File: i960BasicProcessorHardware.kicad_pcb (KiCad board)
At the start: 4 copper layers, 169.9 x 169.8 mm, 75 parts, among them J1 Conn_01x08, J10 Conn_02x39_Odd_Even, J12 Conn_01x03, J13 AVR-ISP-6, J14 Conn_01x06 (Serial Connector), J15 Conn_01x01, J2 Conn_02x05_Odd_Even, J3 Conn_02x05_Odd_Even, J4 Conn_02x05_Odd_Even, J5 Conn_02x16_Odd_Even, J6 Conn_01x03, J7 Conn_01x03, J8 Conn_01x03, J9 Conn_01x11, U1 74HC245, U10 Adafruit_FeatherWing (PSRAM F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, U11 Adafruit_FeatherWing (PSRAM F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, U12 74LS125, U13 74LS04, U14 74LS08, U15 74LS174, U16 SN74LVC245AN, U17 74LS174, U18 ATmega1284P-PU, U2 80960Sx, U3 MCP23S17_SP, U4 MCP23S17_SP, U5 74HC245, U6 74HC573, U7 74HC573, U8 MCP23S17_SP, U9 MCP23S17_SP, X1 CXO_DIP14

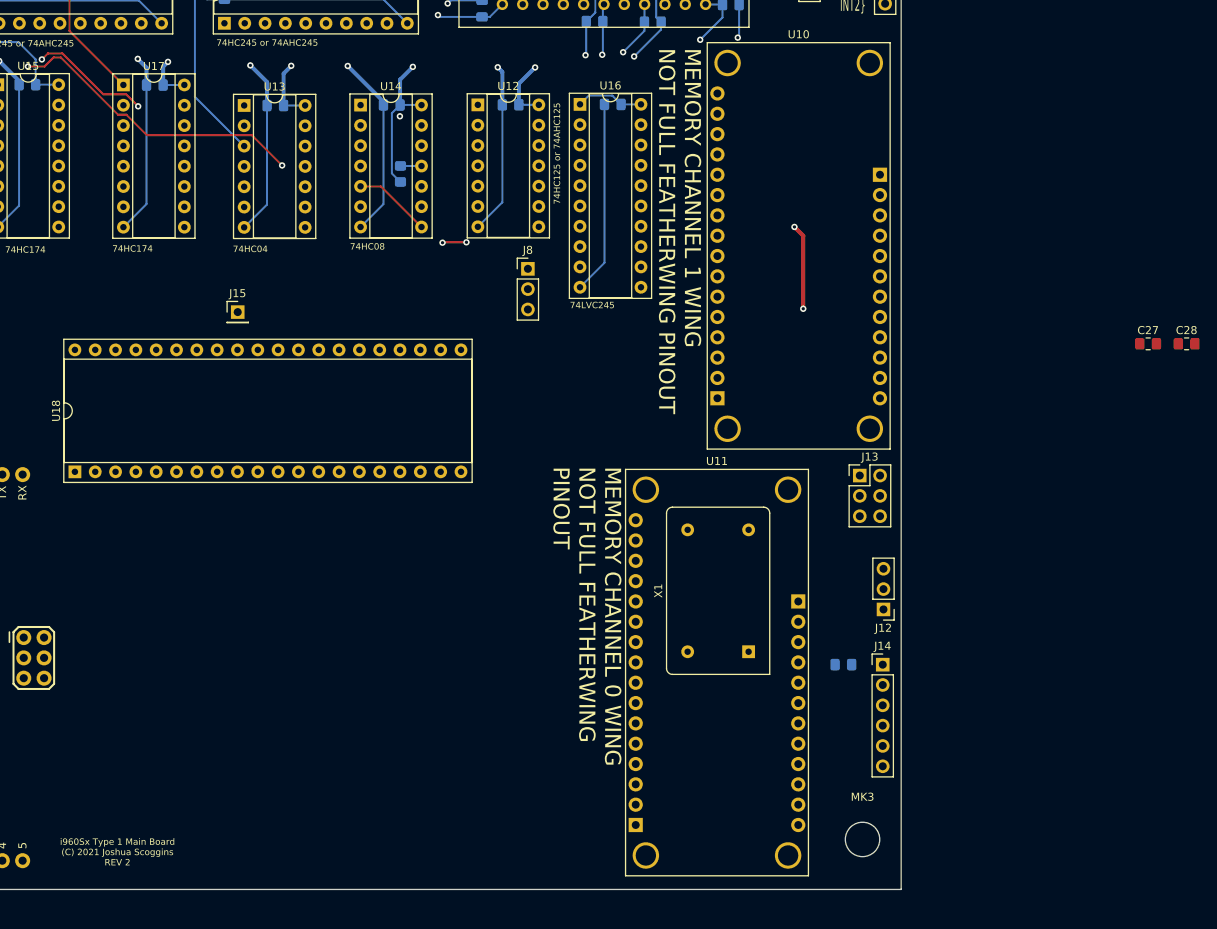
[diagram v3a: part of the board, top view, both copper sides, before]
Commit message: Double headers for each co processor
Added a second coprocessor
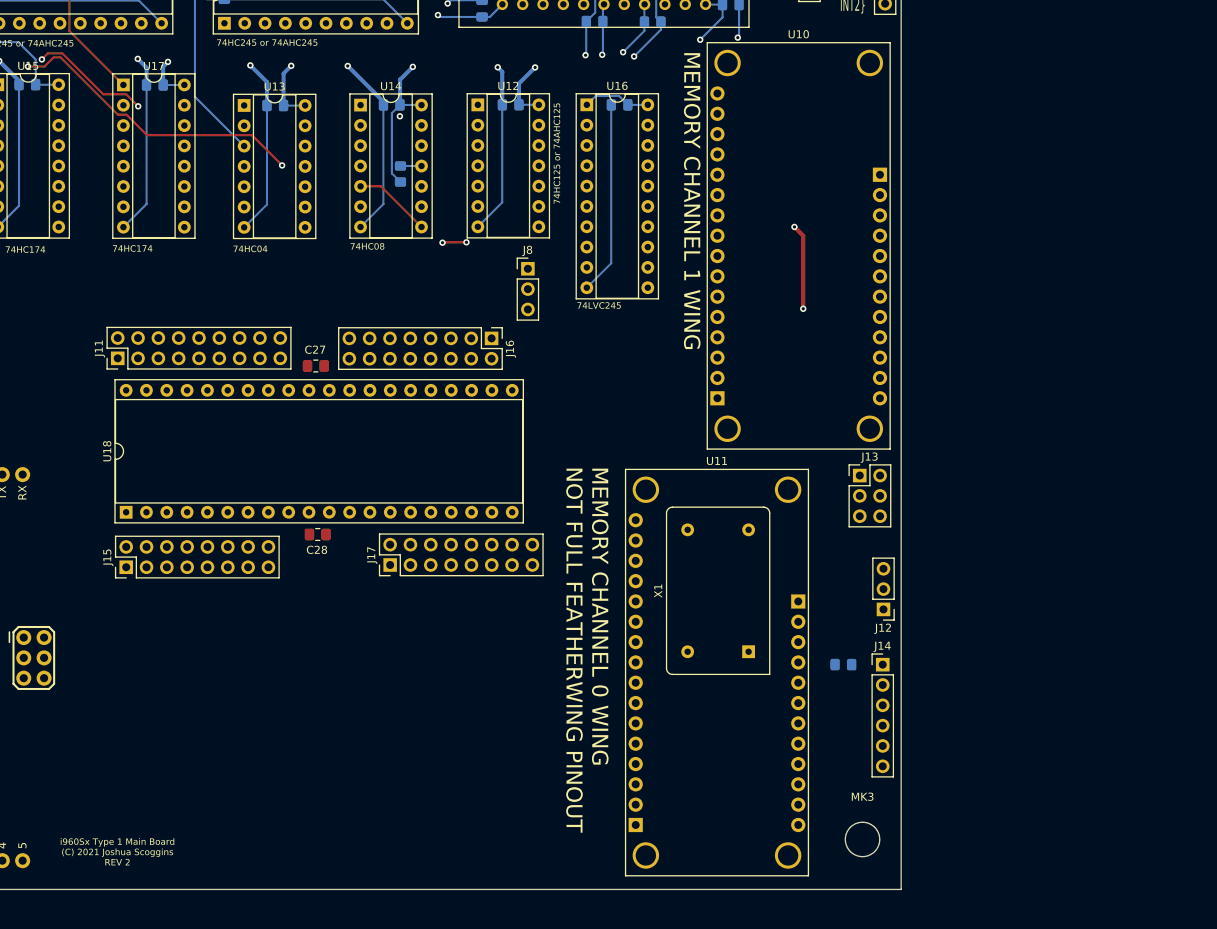
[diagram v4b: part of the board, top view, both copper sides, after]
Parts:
- added J11: Conn_02x09_Odd_Even, Connector_PinHeader_2.54mm:PinHeader_2x09_P2.54mm_Vertical, F.Cu at (88.9, 133.4)
- added J16: Conn_02x08_Odd_Even, Connector_PinHeader_2.54mm:PinHeader_2x08_P2.54mm_Vertical, F.Cu at (135.6, 130.9)
- added J17: Conn_02x08_Odd_Even, Connector_PinHeader_2.54mm:PinHeader_2x08_P2.54mm_Vertical, F.Cu at (123.0, 159.3)
- J15: value Conn_01x01 -> Conn_02x08_Odd_Even; footprint Connector_PinHeader_2.54mm:PinHeader_1x01_P2.54mm_Vertical -> Connector_PinHeader_2.54mm:PinHeader_2x08_P2.54mm_Vertical
- moved C28 111.2 mm to (113.9, 155.5)
- moved C27 104.1 mm to (113.7, 134.4), turned to 180 degrees
- moved J15 34.8 mm to (90.0, 159.6), turned to 90 degrees
- moved U18 8.16 mm to (90.0, 152.7)
- moved C22 0.86 mm to (151.7, 101.8)
- moved U16 0.86 mm to (147.6, 101.7)
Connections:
- net /Sheet7D8CCC79/PD0 renamed /COPROC0_PD0
- net /Sheet7D8CCC79/PD1 renamed /COPROC0_PD1
- J13 pad 1: /Sheet7D8CCC79/PB6 -> /COPROC0_PB6
- J13 pad 3: /Sheet7D8CCC79/PB7 -> /COPROC0_PB7
- J13 pad 4: /Sheet7D8CCC79/PB5 -> /COPROC0_PB5
- J15 pad 1: /Sheet7D8CCC79/AREF -> /COPROC0_PB0
- U18 pad 1: /Sheet7D8CCC79/PB0 -> /COPROC0_PB0
- U18 pad 16: /Sheet7D8CCC79/PD2 -> /COPROC0_PD2
- U18 pad 17: /Sheet7D8CCC79/PD3 -> /COPROC0_PD3
- U18 pad 18: /Sheet7D8CCC79/PD4 -> /COPROC0_PD4
- U18 pad 19: /Sheet7D8CCC79/PD5 -> /COPROC0_PD5
- U18 pad 2: /Sheet7D8CCC79/PB1 -> /COPROC0_PB1
- U18 pad 20: /Sheet7D8CCC79/PD6 -> /COPROC0_PD6
- U18 pad 21: /Sheet7D8CCC79/PD7 -> /COPROC0_PD7
- U18 pad 22: /Sheet7D8CCC79/PC0 -> /COPROC0_PC0
- U18 pad 23: /Sheet7D8CCC79/PC1 -> /COPROC0_PC1
- U18 pad 24: /Sheet7D8CCC79/PC2 -> /COPROC0_PC2
- U18 pad 25: /Sheet7D8CCC79/PC3 -> /COPROC0_PC3
- U18 pad 26: /Sheet7D8CCC79/PC4 -> /COPROC0_PC4
- U18 pad 27: /Sheet7D8CCC79/PC5 -> /COPROC0_PC5
- U18 pad 28: /Sheet7D8CCC79/PC6 -> /COPROC0_PC6
- U18 pad 29: /Sheet7D8CCC79/PC7 -> /COPROC0_PC7
- U18 pad 3: /Sheet7D8CCC79/PB2 -> /COPROC0_PB2
- U18 pad 32: /Sheet7D8CCC79/AREF -> /COPROC0_AREF
- U18 pad 33: /Sheet7D8CCC79/PA7 -> /COPROC0_PA7
- U18 pad 34: /Sheet7D8CCC79/PA6 -> /COPROC0_PA6
- U18 pad 35: /Sheet7D8CCC79/PA5 -> /COPROC0_PA5
- U18 pad 36: /Sheet7D8CCC79/PA4 -> /COPROC0_PA4
- U18 pad 37: /Sheet7D8CCC79/PA3 -> /COPROC0_PA3
- U18 pad 38: /Sheet7D8CCC79/PA2 -> /COPROC0_PA2
- U18 pad 39: /Sheet7D8CCC79/PA1 -> /COPROC0_PA1
- U18 pad 4: /Sheet7D8CCC79/PB3 -> /COPROC0_PB3
- U18 pad 40: /Sheet7D8CCC79/PA0 -> /COPROC0_PA0
- U18 pad 5: /Sheet7D8CCC79/PB4 -> /COPROC0_PB4
- U18 pad 6: /Sheet7D8CCC79/PB5 -> /COPROC0_PB5
- U18 pad 7: /Sheet7D8CCC79/PB6 -> /COPROC0_PB6
- U18 pad 8: /Sheet7D8CCC79/PB7 -> /COPROC0_PB7
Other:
- board text added: "MEMORY CHANNEL 1 WING"
- board text removed: "MEMORY CHANNEL 1 WING NOT FULL FEATHERWING PINOUT"

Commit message: Keep futzing with the design
Added a missing +5v power source to the x4 coprocessor schematic
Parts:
- added C30: 0.1uF, Capacitor_SMD:C_0805_2012Metric_Pad1.18x1.45mm_HandSolder, F.Cu at (219.1, 161.7)
- added C31: 0.1uF, Capacitor_SMD:C_0805_2012Metric_Pad1.18x1.45mm_HandSolder, F.Cu at (255.0, 109.2)
- added C32: 0.1uF, Capacitor_SMD:C_0805_2012Metric_Pad1.18x1.45mm_HandSolder, F.Cu at (243.1, 118.9)
- added J18: Conn_02x09_Odd_Even, Connector_PinHeader_2.54mm:PinHeader_2x09_P2.54mm_Vertical, F.Cu at (323.4, 110.0)
- added J19: Conn_02x08_Odd_Even, Connector_PinHeader_2.54mm:PinHeader_2x08_P2.54mm_Vertical, F.Cu at (330.6, 110.0)
- added J20: Conn_02x08_Odd_Even, Connector_PinHeader_2.54mm:PinHeader_2x08_P2.54mm_Vertical, F.Cu at (337.8, 110.0)
- added J21: Conn_02x08_Odd_Even, Connector_PinHeader_2.54mm:PinHeader_2x08_P2.54mm_Vertical, F.Cu at (345.0, 110.0)
- added J22: Conn_01x03, Connector_PinHeader_2.54mm:PinHeader_1x03_P2.54mm_Vertical, F.Cu at (243.0, 110.0)
- added J23: AVR-ISP-6, Connector_PinHeader_2.54mm:PinHeader_2x03_P2.54mm_Vertical, F.Cu at (247.7, 110.0)
- added J24: Conn_01x06 (Serial Connector), Connector_PinHeader_2.54mm:PinHeader_1x06_P2.54mm_Vertical, F.Cu at (238.4, 110.0)
- added U19: ATmega1284P-PU, Package_DIP:DIP-40_W15.24mm_Socket, F.Cu at (90.0, 186.5)
- moved J4 69.7 mm to (112.8, 35.0), turned to 90 degrees
- moved J3 66.7 mm to (41.4, 32.2)
- moved J2 24.6 mm to (103.1, 32.5)
- moved B1 20.0 mm to (54.9, 152.2)
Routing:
- net /RX0: track 127.8 -> 2.54 mm, vias 3 -> 0
- net /TX0: track 123.2 -> 2.54 mm, vias 3 -> 0
- net /~MCU_RESET: track 121.7 -> 2.54 mm
- net /VIN: track 115.8 -> 2.54 mm
- net /~SD_CS: track 86.4 -> 2.54 mm, vias 2 -> 0
- net /SCL: track 82.3 -> 2.54 mm, vias 2 -> 0
- net /TFT_DC: track 82.3 -> 2.54 mm, vias 2 -> 0
- net /~TFT_CS: track 81.4 -> 2.54 mm, vias 2 -> 0
- net /SDA: track 80.8 -> 2.54 mm, vias 1 -> 0
- net /AREF: track 37.3 -> 2.54 mm
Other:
- board text added: "i960Sx Type 1 Main Board (C) 2021 Joshua Scoggins REV 3"
- board text removed: "i960Sx Type 1 Main Board (C) 2021 Joshua Scoggins REV 2"

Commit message: Rudimentary layout
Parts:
- removed J21: Conn_02x08_Odd_Even, Connector_PinHeader_2.54mm:PinHeader_2x08_P2.54mm_Vertical
- C32: moved to B.Cu
- J19: value Conn_02x08_Odd_Even -> Conn_02x16_Odd_Even; footprint Connector_PinHeader_2.54mm:PinHeader_2x08_P2.54mm_Vertical -> Connector_PinHeader_2.54mm:PinHeader_2x16_P2.54mm_Vertical
- moved J18 302.0 mm to (34.4, 197.6), turned to 90 degrees
- moved J19 284.2 mm to (60.2, 197.6), turned to 90 degrees
- moved J20 206.9 mm to (149.1, 194.8), turned to 270 degrees
- moved C31 171.1 mm to (103.7, 189.2)
- moved J24 149.0 mm to (117.9, 197.6), turned to 270 degrees
- moved C32 145.8 mm to (117.9, 193.6), turned to 90 degrees
- moved J23 120.7 mm to (160.8, 193.9), turned to 90 degrees
- moved C30 115.6 mm to (103.6, 168.2), turned to 180 degrees
- moved J22 102.5 mm to (169.5, 181.3), turned to 180 degrees
- moved B1 12.3 mm to (43.4, 156.6)
- moved J11 11.4 mm to (77.9, 130.3)
- moved U19 10.3 mm to (79.6, 186.3)
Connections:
- C27 pad 1: Net-(C27-Pad1) -> +5V
- C30 pad 1: Net-(C30-Pad1) -> +5V
- U18 pad 30: Net-(C27-Pad1) -> +5V
- U19 pad 30: Net-(C30-Pad1) -> +5V
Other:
- board text added: "MEMORY CHANNEL 0 WING"
- board text removed: "MEMORY CHANNEL 0 WING NOT FULL FEATHERWING PINOUT"

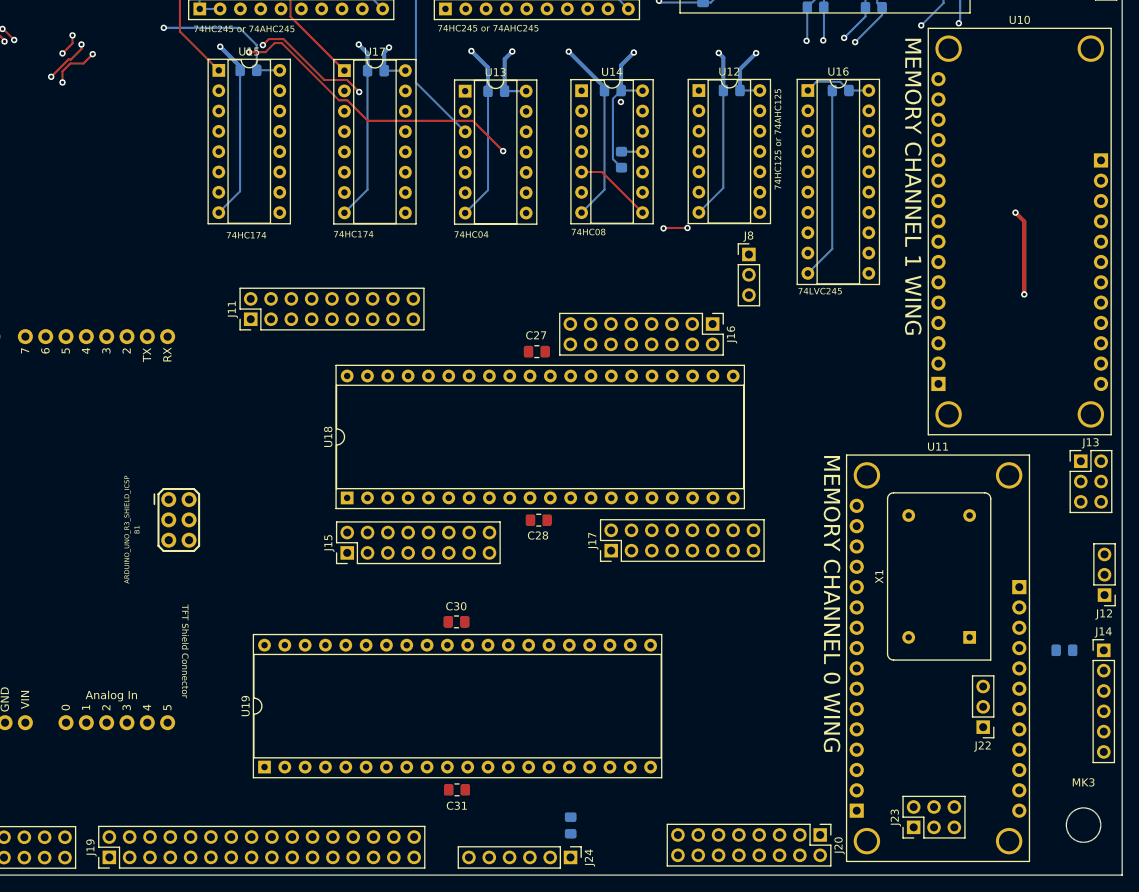
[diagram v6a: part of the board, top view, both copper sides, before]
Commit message: Get the two co processors laid out properly and start wiring it up
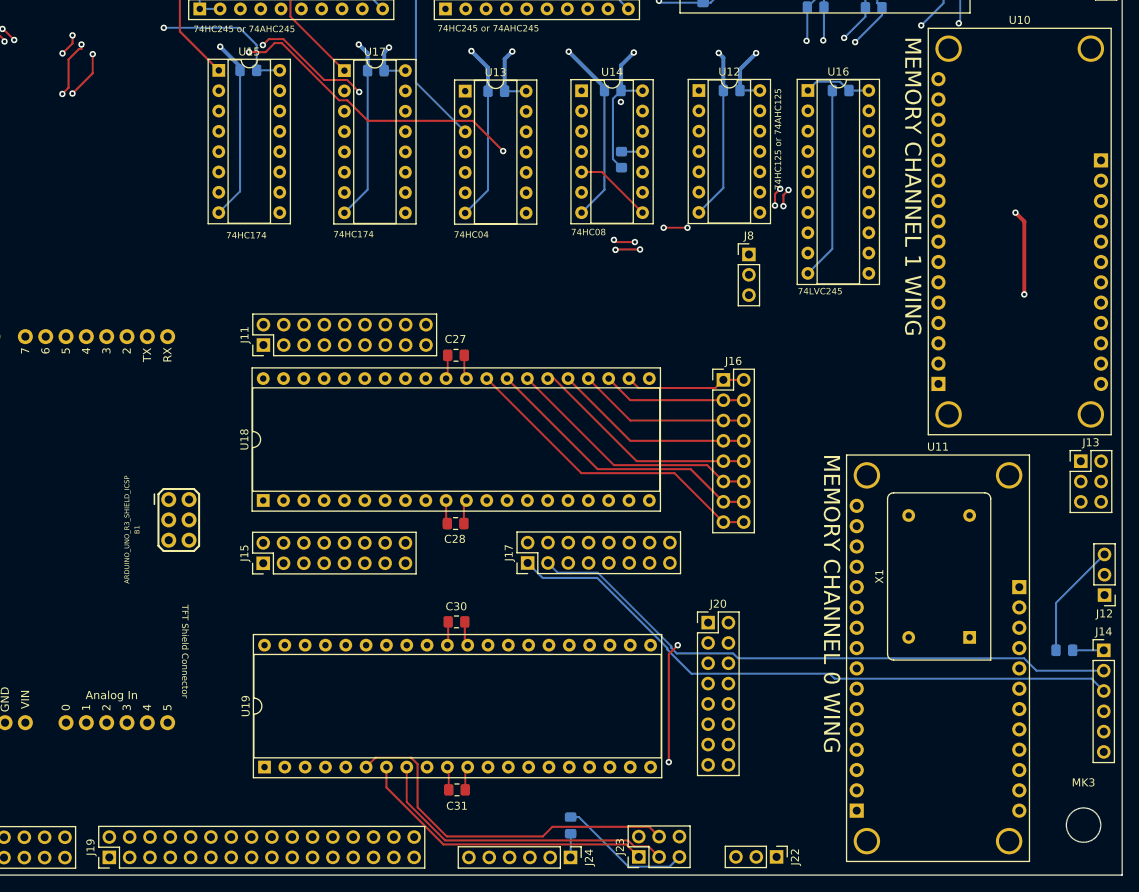
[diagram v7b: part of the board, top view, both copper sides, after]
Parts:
- moved J23 34.6 mm to (126.4, 197.6)
- moved J22 30.5 mm to (143.6, 197.6), turned to 270 degrees
- moved J20 30.0 mm to (135.1, 168.3), turned to 0 degrees
- moved J15 10.6 mm to (79.5, 160.8)
- moved J17 10.6 mm to (112.5, 160.8)
- moved U18 10.5 mm to (79.5, 153.0)
- moved C28 10.4 mm to (103.5, 155.9)
- moved C27 10.1 mm to (103.6, 134.9)
- moved J16 7.11 mm to (137.0, 137.9), turned to 0 degrees
- moved J11 3.60 mm to (79.5, 133.6)
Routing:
- net /~MCU_RESET: track 2.54 -> 206.7 mm
- net /COPROC0_PB5: track 0.00 -> 105.6 mm
- net /MOSI0: track 254.0 -> 358.4 mm, vias 3 -> 5
- net /SCK1: track 63.3 -> 167.3 mm, vias 2 -> 4
- net /MOSI1: track 64.2 -> 165.9 mm, vias 3 -> 5
- net /SCK0: track 253.3 -> 355.1 mm, vias 2 -> 4
- net /COPROC0_PB6: track 0.00 -> 97.5 mm
- net /COPROC0_PB7: track 0.00 -> 97.0 mm
- net /~3V_PSRAM_EN1: track 0.00 -> 91.3 mm
- net /~3V_PSRAM_EN2: track 0.00 -> 91.3 mm
- net /3V_MISO0: track 0.00 -> 89.4 mm
- net /Sheet7D8CCC79/~RESET: track 0.00 -> 88.9 mm
- net /COPROC0_PD0: track 0.00 -> 86.6 mm
- net /EXTCLK: track 0.00 -> 84.6 mm
- net /COPROC0_PD1: track 0.00 -> 83.0 mm
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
